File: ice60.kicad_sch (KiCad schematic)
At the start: 31 parts, among them J1 SWD, J2 JST SH 4-pin, SW0 SW_Push, U1 RP2040, U2 W25Q128JVS, U3 XC6206PxxxMR, U4 SRV05-4, Y1 12MHz

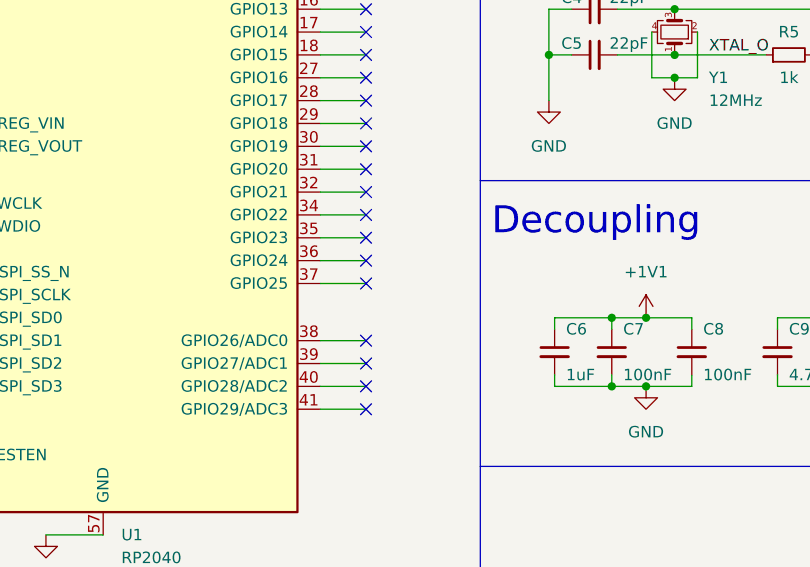
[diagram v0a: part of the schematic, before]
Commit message: route columns and row 0
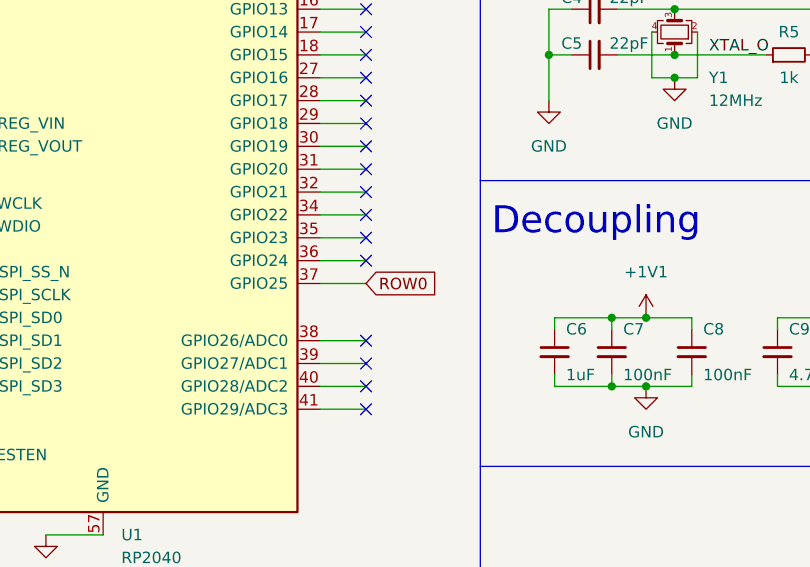
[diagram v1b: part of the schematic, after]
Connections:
- net ROW0: now reaches U1.37 (GPIO25)
- no-connect marks 32 -> 31
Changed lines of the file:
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@@
   (no_connect (at 88.9 88.9))
   (no_connect (at 88.9 40.64))
-  (no_connect (at 88.9 96.52))
   (no_connect (at 88.9 81.28))
   (no_connect (at 88.9 78.74))
@@
     )
   )
+  (global_label "ROW0" (shape input) (at 88.9 96.52 0) (fields_autoplaced)
+    (effects (font (size 1.27 1.27)) (justify left))
+    (property "Intersheet References" "${INTERSHEET_REFS}" (id 0) (at 96.5745 96.4406 0)
+      (effects (font (size 1.27 1.27)) (justify left) hide)
+    )
+  )
   (global_label "SWD" (shape input) (at 43.18 90.17 180) (fields_autoplaced)
     (effects (font (size 1.27 1.27)) (justify right))
@@
   (symbol (lib_id "power:+5V") (at 240.03 20.32 0) (unit 1)
     (in_bom yes) (on_board yes)
-    (property "Reference" "#PWR?" (id 0) (at 240.03 24.13 0)
+    (property "Reference" "#PWR0104" (id 0) (at 240.03 24.13 0)
       (effects (font (size 1.27 1.27)) hide)
     )
@@
     )
     (path "/98dd4e45-1185-44d2-8220-7a892da24295"
-      (reference "#PWR?") (unit 1) (value "+5V") (footprint "")
+      (reference "#PWR0104") (unit 1) (value "+5V") (footprint "")
     )
     (path "/56077389-3dc3-4dac-9d26-70524308becc"

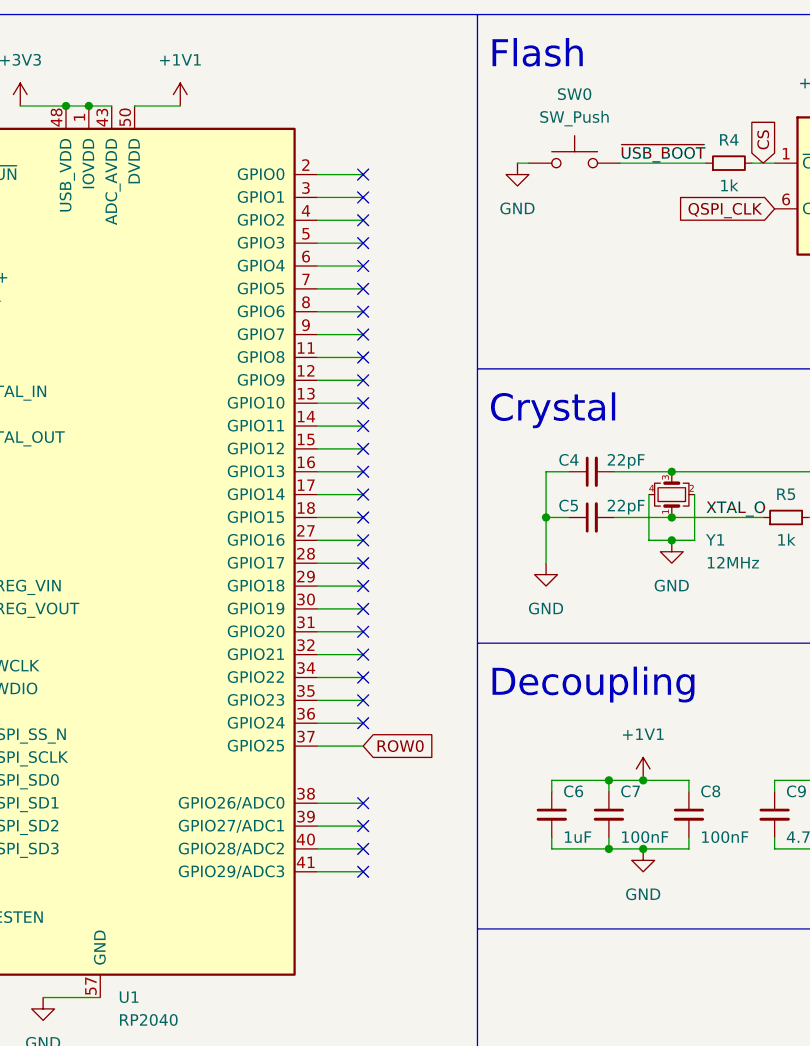
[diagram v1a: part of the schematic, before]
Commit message: complete initial routing
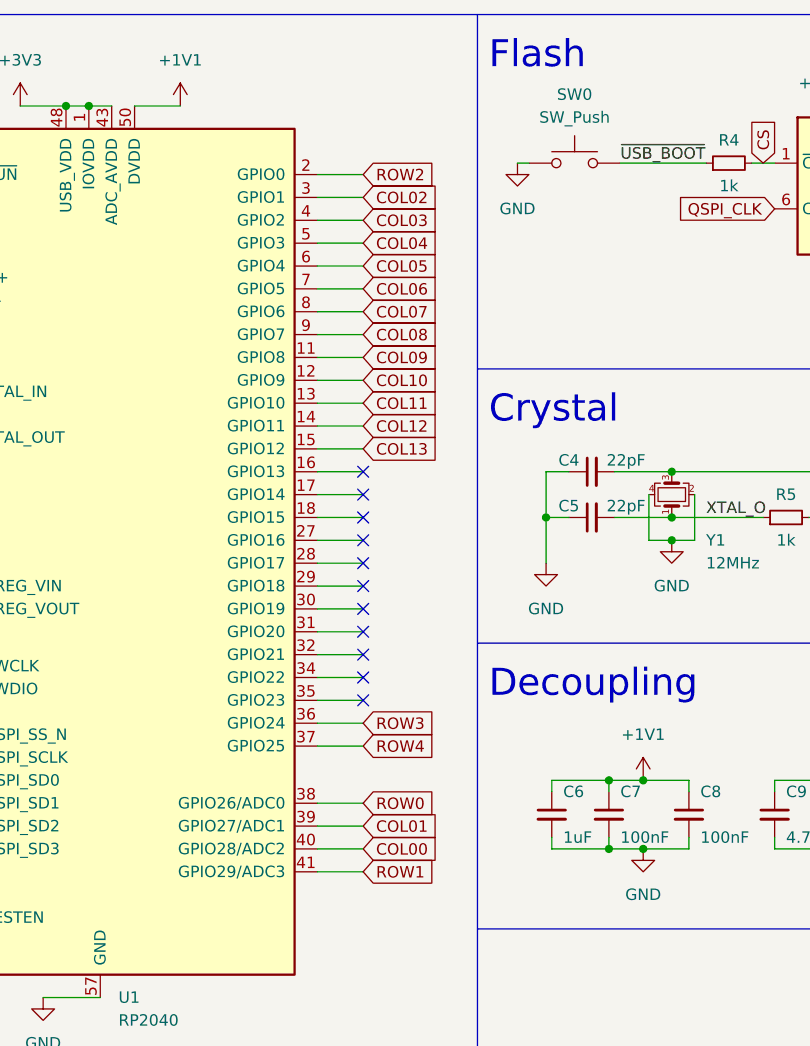
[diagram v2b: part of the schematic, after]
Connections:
- net ROW0: now also U1.38 (GPIO26/ADC0); no longer U1.37 (GPIO25)
- net COL09: now reaches U1.11 (GPIO8)
- net COL10: now reaches U1.12 (GPIO9)
- net COL11: now reaches U1.13 (GPIO10)
- net COL12: now reaches U1.14 (GPIO11)
- net COL13: now reaches U1.15 (GPIO12)
- net ROW2: now reaches U1.2 (GPIO0)
- net COL02: now reaches U1.3 (GPIO1)
- net ROW3: now reaches U1.36 (GPIO24)
- net COL01: now reaches U1.39 (GPIO27/ADC1)
- net COL03: now reaches U1.4 (GPIO2)
- net COL00: now reaches U1.40 (GPIO28/ADC2)
- net ROW1: now reaches U1.41 (GPIO29/ADC3)
- net COL04: now reaches U1.5 (GPIO3)
- net COL05: now reaches U1.6 (GPIO4)
- net COL06: now reaches U1.7 (GPIO5)
- net COL07: now reaches U1.8 (GPIO6)
- net COL08: now reaches U1.9 (GPIO7)
- new net ROW4: U1.37 (GPIO25)
- no-connect marks 31 -> 13
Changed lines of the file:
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@@
   (junction (at 148.59 100.33) (diameter 0) (color 0 0 0 0)
   )
-  (no_connect (at 88.9 55.88))
-  (no_connect (at 88.9 43.18))
   (no_connect (at 88.9 68.58))
-  (no_connect (at 88.9 110.49))
-  (no_connect (at 88.9 35.56))
-  (no_connect (at 88.9 63.5))
   (no_connect (at 227.33 33.02))
   (no_connect (at 88.9 66.04))
-  (no_connect (at 88.9 105.41))
-  (no_connect (at 88.9 91.44))
   (no_connect (at 88.9 88.9))
-  (no_connect (at 88.9 40.64))
   (no_connect (at 88.9 81.28))
   (no_connect (at 88.9 78.74))
   (no_connect (at 88.9 86.36))
   (no_connect (at 252.73 38.1))
-  (no_connect (at 88.9 50.8))
-  (no_connect (at 88.9 102.87))
-  (no_connect (at 88.9 60.96))
-  (no_connect (at 88.9 107.95))
-  (no_connect (at 88.9 33.02))
-  (no_connect (at 88.9 45.72))
-  (no_connect (at 88.9 58.42))
+  (no_connect (at 88.9 91.44))
   (no_connect (at 88.9 83.82))
-  (no_connect (at 88.9 38.1))
   (no_connect (at 88.9 73.66))
-  (no_connect (at 88.9 53.34))
   (no_connect (at 88.9 71.12))
-  (no_connect (at 88.9 93.98))
-  (no_connect (at 88.9 48.26))
   (no_connect (at 88.9 76.2))
   (polyline (pts (xy 15.24 15.24) (xy 15.24 134.62))
@@
     )
   )
+  (global_label "ROW0" (shape input) (at 88.9 102.87 0) (fields_autoplaced)
+    (effects (font (size 1.27 1.27)) (justify left))
+    (property "Intersheet References" "${INTERSHEET_REFS}" (id 0) (at 96.5745 102.7906 0)
+      (effects (font (size 1.27 1.27)) (justify left) hide)
+    )
+  )
+  (global_label "ROW2" (shape input) (at 88.9 33.02 0) (fields_autoplaced)
+    (effects (font (size 1.27 1.27)) (justify left))
+    (property "Intersheet References" "${INTERSHEET_REFS}" (id 0) (at 96.5745 32.9406 0)
+      (effects (font (size 1.27 1.27)) (justify left) hide)
+    )
+  )
   (global_label "D_N" (shape input) (at 27.94 46.99 180) (fields_autoplaced)
     (effects (font (size 1.27 1.27)) (justify right))
@@
     )
   )
+  (global_label "COL11" (shape input) (at 88.9 58.42 0) (fields_autoplaced)
+    (effects (font (size 1.27 1.27)) (justify left))
+    (property "Intersheet References" "${INTERSHEET_REFS}" (id 0) (at 97.3607 58.3406 0)
+      (effects (font (size 1.27 1.27)) (justify left) hide)
+    )
+  )
+  (global_label "COL08" (shape input) (at 88.9 50.8 0) (fields_autoplaced)
+    (effects (font (size 1.27 1.27)) (justify left))
+    (property "Intersheet References" "${INTERSHEET_REFS}" (id 0) (at 97.3607 50.7206 0)
+      (effects (font (size 1.27 1.27)) (justify left) hide)
+    )
+  )
   (global_label "XTAL_OUT" (shape input) (at 43.18 62.23 180) (fields_autoplaced)
     (effects (font (size 1.27 1.27)) (justify right))
@@
     )
   )
+  (global_label "COL00" (shape input) (at 88.9 107.95 0) (fields_autoplaced)
+    (effects (font (size 1.27 1.27)) (justify left))
+    (property "Intersheet References" "${INTERSHEET_REFS}" (id 0) (at 97.3607 107.8706 0)
+      (effects (font (size 1.27 1.27)) (justify left) hide)
+    )
+  )
   (global_label "SD1" (shape input) (at 43.18 102.87 180) (fields_autoplaced)
     (effects (font (size 1.27 1.27)) (justify right))
@@
     )
   )
+  (global_label "COL01" (shape input) (at 88.9 105.41 0) (fields_autoplaced)
+    (effects (font (size 1.27 1.27)) (justify left))
+    (property "Intersheet References" "${INTERSHEET_REFS}" (id 0) (at 97.3607 105.3306 0)
+      (effects (font (size 1.27 1.27)) (justify left) hide)
+    )
+  )
   (global_label "SWCLK" (shape input) (at 172.72 77.47 0) (fields_autoplaced)
     (effects (font (size 1.27 1.27)) (justify left))
@@
     )
   )
+  (global_label "COL04" (shape input) (at 88.9 40.64 0) (fields_autoplaced)
+    (effects (font (size 1.27 1.27)) (justify left))
+    (property "Intersheet References" "${INTERSHEET_REFS}" (id 0) (at 97.3607 40.5606 0)
+      (effects (font (size 1.27 1.27)) (justify left) hide)
+    )
+  )
   (global_label "CS" (shape input) (at 43.18 95.25 180) (fields_autoplaced)
     (effects (font (size 1.27 1.27)) (justify right))
@@
     )
   )
+  (global_label "COL03" (shape input) (at 88.9 38.1 0) (fields_autoplaced)
+    (effects (font (size 1.27 1.27)) (justify left))
+    (property "Intersheet References" "${INTERSHEET_REFS}" (id 0) (at 97.3607 38.0206 0)
+      (effects (font (size 1.27 1.27)) (justify left) hide)
+    )
+  )
+  (global_label "COL13" (shape input) (at 88.9 63.5 0) (fields_autoplaced)
+    (effects (font (size 1.27 1.27)) (justify left))
+    (property "Intersheet References" "${INTERSHEET_REFS}" (id 0) (at 97.3607 63.4206 0)
+      (effects (font (size 1.27 1.27)) (justify left) hide)
+    )
+  )
+  (global_label "COL02" (shape input) (at 88.9 35.56 0) (fields_autoplaced)
+    (effects (font (size 1.27 1.27)) (justify left))
+    (property "Intersheet References" "${INTERSHEET_REFS}" (id 0) (at 97.3607 35.4806 0)
+      (effects (font (size 1.27 1.27)) (justify left) hide)
+    )
+  )
+  (global_label "COL05" (shape input) (at 88.9 43.18 0) (fields_autoplaced)
+    (effects (font (size 1.27 1.27)) (justify left))
+    (property "Intersheet References" "${INTERSHEET_REFS}" (id 0) (at 97.3607 43.1006 0)
+      (effects (font (size 1.27 1.27)) (justify left) hide)
+    )
+  )
   (global_label "D_P" (shape input) (at 252.73 33.02 0) (fields_autoplaced)
     (effects (font (size 1.27 1.27)) (justify left))
@@
     )
   )
+  (global_label "ROW3" (shape input) (at 88.9 93.98 0) (fields_autoplaced)
+    (effects (font (size 1.27 1.27)) (justify left))
+    (property "Intersheet References" "${INTERSHEET_REFS}" (id 0) (at 96.5745 93.9006 0)
+      (effects (font (size 1.27 1.27)) (justify left) hide)
+    )
+  )
+  (global_label "COL09" (shape input) (at 88.9 53.34 0) (fields_autoplaced)
+    (effects (font (size 1.27 1.27)) (justify left))
+    (property "Intersheet References" "${INTERSHEET_REFS}" (id 0) (at 97.3607 53.2606 0)
+      (effects (font (size 1.27 1.27)) (justify left) hide)
+    )
+  )
   (global_label "D_P" (shape input) (at 27.94 44.45 180) (fields_autoplaced)
     (effects (font (size 1.27 1.27)) (justify right))
@@
     )
   )
+  (global_label "ROW4" (shape input) (at 88.9 96.52 0) (fields_autoplaced)
+    (effects (font (size 1.27 1.27)) (justify left))
+    (property "Intersheet References" "${INTERSHEET_REFS}" (id 0) (at 96.5745 96.4406 0)
+      (effects (font (size 1.27 1.27)) (justify left) hide)
+    )
+  )
+  (global_label "COL06" (shape input) (at 88.9 45.72 0) (fields_autoplaced)
+    (effects (font (size 1.27 1.27)) (justify left))
+    (property "Intersheet References" "${INTERSHEET_REFS}" (id 0) (at 97.3607 45.6406 0)
+      (effects (font (size 1.27 1.27)) (justify left) hide)
+    )
+  )
   (global_label "CS" (shape input) (at 133.35 31.75 90) (fields_autoplaced)
     (effects (font (size 1.27 1.27)) (justify left))
@@
     )
   )
+  (global_label "COL07" (shape input) (at 88.9 48.26 0) (fields_autoplaced)
+    (effects (font (size 1.27 1.27)) (justify left))
+    (property "Intersheet References" "${INTERSHEET_REFS}" (id 0) (at 97.3607 48.1806 0)
+      (effects (font (size 1.27 1.27)) (justify left) hide)
+    )
+  )
   (global_label "D_N" (shape input) (at 218.44 69.85 0) (fields_autoplaced)
     (effects (font (size 1.27 1.27)) (justify left))
@@
     )
   )
-  (global_label "ROW0" (shape input) (at 88.9 96.52 0) (fields_autoplaced)
-    (effects (font (size 1.27 1.27)) (justify left))
-    (property "Intersheet References" "${INTERSHEET_REFS}" (id 0) (at 96.5745 96.4406 0)
+  (global_label "ROW1" (shape input) (at 88.9 110.49 0) (fields_autoplaced)
+    (effects (font (size 1.27 1.27)) (justify left))
+    (property "Intersheet References" "${INTERSHEET_REFS}" (id 0) (at 96.5745 110.4106 0)
       (effects (font (size 1.27 1.27)) (justify left) hide)
     )
@@
       (effects (font (size 1.27 1.27)) (justify left) hide)
     )
+  )
+  (global_label "COL10" (shape input) (at 88.9 55.88 0) (fields_autoplaced)
+    (effects (font (size 1.27 1.27)) (justify left))
+    (property "Intersheet References" "${INTERSHEET_REFS}" (id 0) (at 97.3607 55.8006 0)
+      (effects (font (size 1.27 1.27)) (justify left) hide)
+    )
+  )
+  (global_label "COL12" (shape input) (at 88.9 60.96 0) (fields_autoplaced)
+    (effects (font (size 1.27 1.27)) (justify left))
+    (property "Intersheet References" "${INTERSHEET_REFS}" (id 0) (at 97.3607 60.8806 0)
+      (effects (font (size 1.27 1.27)) (justify left) hide)
+    )

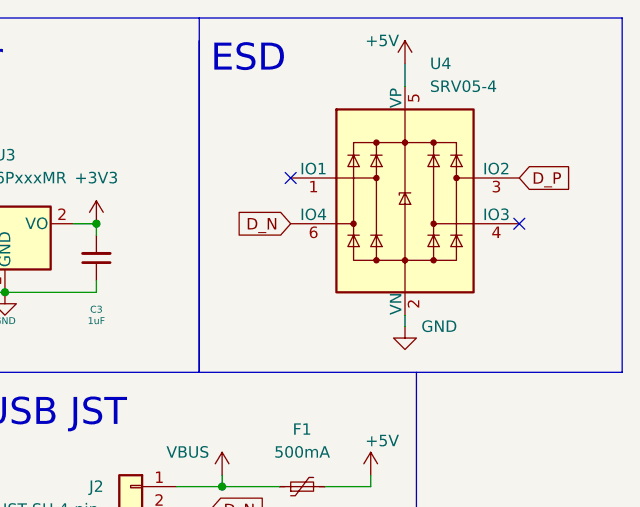
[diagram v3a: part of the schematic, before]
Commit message: reroute USB data & several tweaks
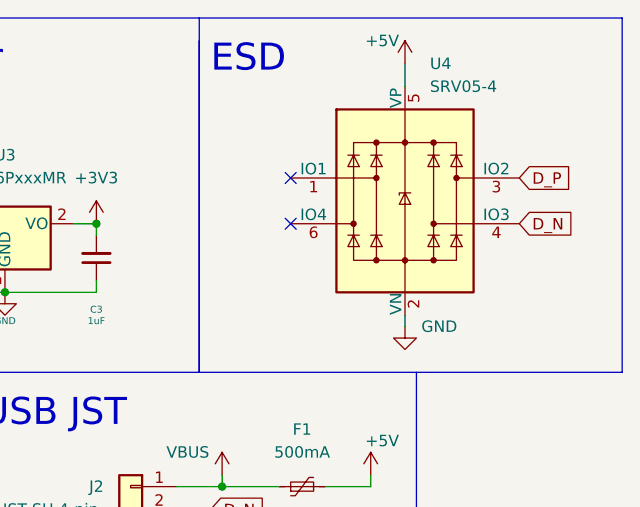
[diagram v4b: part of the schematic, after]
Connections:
- net D_N: now also U4.4 (IO3); no longer U4.6 (IO4)
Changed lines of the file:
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@@
   (no_connect (at 88.9 78.74))
   (no_connect (at 88.9 86.36))
-  (no_connect (at 252.73 38.1))
+  (no_connect (at 227.33 38.1))
   (no_connect (at 88.9 91.44))
   (no_connect (at 88.9 83.82))
@@
     )
   )
-  (global_label "D_N" (shape input) (at 227.33 38.1 180) (fields_autoplaced)
-    (effects (font (size 1.27 1.27)) (justify right))
-    (property "Intersheet References" "${INTERSHEET_REFS}" (id 0) (at 221.3488 38.0206 0)
-      (effects (font (size 1.27 1.27)) (justify right) hide)
-    )
-  )
+  (global_label "D_N" (shape input) (at 252.73 38.1 0) (fields_autoplaced)
+    (effects (font (size 1.27 1.27)) (justify left))
+    (property "Intersheet References" "${INTERSHEET_REFS}" (id 0) (at 258.7112 38.1794 0)
+      (effects (font (size 1.27 1.27)) (justify left) hide)
+    )
+  )
